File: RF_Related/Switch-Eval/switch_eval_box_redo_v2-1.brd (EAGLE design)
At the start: 54.6 x 48.6 mm, 20 parts, among them IC1 SN74LVC2G17DBVT, IC2 HSWA2-30DR+, IC4 MAX8878EUK28+T, J1 171856-0002, J2 M20-7830246, X1 SMA-142-0701-801/806, X2 SMA-142-0701-801/806, X3 SMA-142-0701-801/806

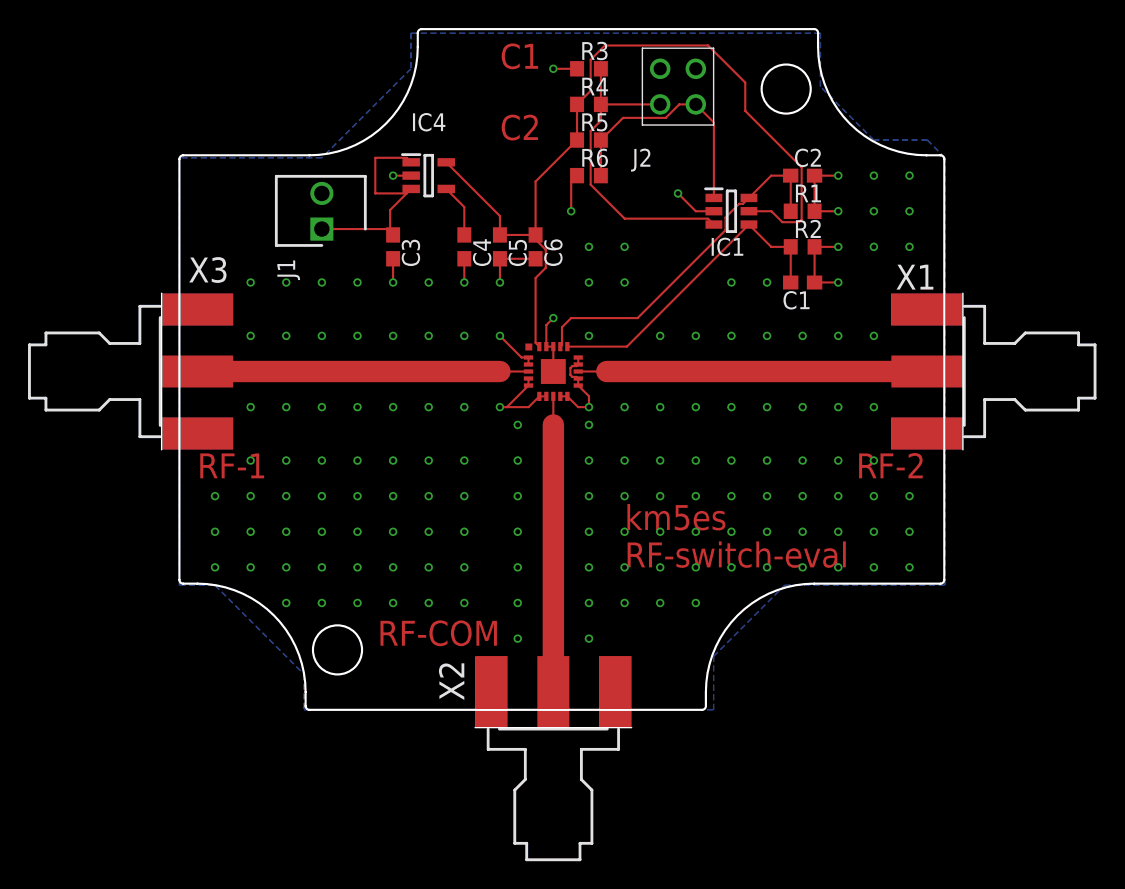
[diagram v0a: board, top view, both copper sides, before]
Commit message: made a new revision of the simple RF switch and sent it to fab.
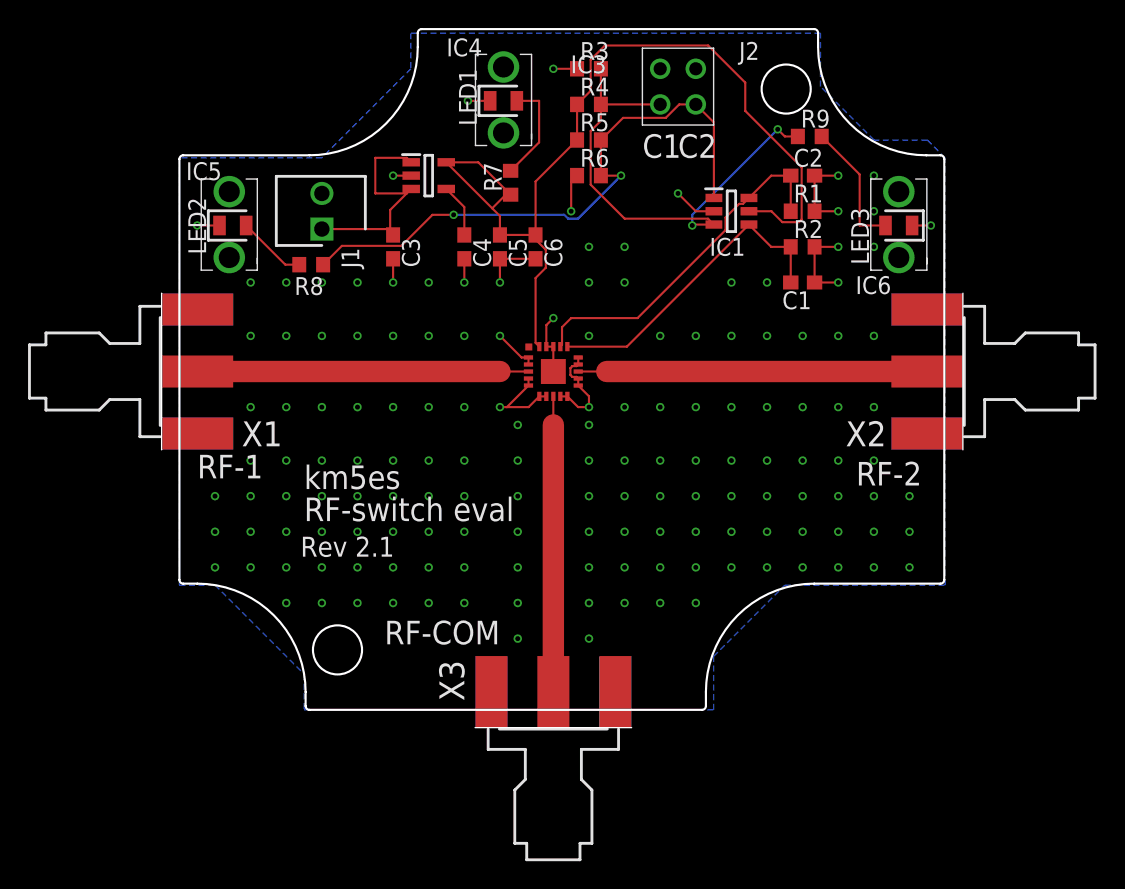
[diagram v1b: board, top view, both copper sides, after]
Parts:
- added IC3, IC5, IC6: VLPR-24-858-2, VLPR-24-858-2:VLPR248582
- added LED1: APT2012LVBC_D, APT2012LVBC_D:LEDC2012X85N
- added LED2, LED3: APT2012LZGCK, APT2012LZGCK:LEDC2012X85N
- added R7, R8, R9: 430, rcl:R0603
- moved X1 57.2 mm to (-1.27, 24.1), turned to 0 degrees
- moved X2 38.7 mm to (55.9, 24.1), turned to 180 degrees
- moved X3 37.8 mm to (26.7, -1.27), turned to 90 degrees
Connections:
- new net N$13: LED2.2, R8.2
- new net N$5: LED1.2, R7.2
- new net N$6: LED3.2, R9.2
- net GND: now also LED1.1, LED2.1, LED3.1
- net N$1: now also R9.1
- net N$10: now also X2.1; no longer X1.1
- net N$12: now also X3.1; no longer X2.1
- net N$4: now also R8.1
- net N$7: now also R7.1
- net N$8: now also X1.1; no longer X3.1
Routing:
- net N$4: track 17.6 -> 43.1 mm, vias 0 -> 2
- net N$1: track 22.8 -> 35.4 mm, vias 0 -> 2
- net N$6: track 0.00 -> 9.31 mm
- net N$5: track 0.00 -> 7.42 mm
- net N$7: track 60.2 -> 67.5 mm
- net N$13: track 0.00 -> 4.95 mm
- net GND: track 49.4 -> 54.0 mm
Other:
- board text added: "RF-switch eval"
- board text added: "Rev 2.1"
- board text added: "km5es"
- board text removed: "km5es RF-switch-eval"
